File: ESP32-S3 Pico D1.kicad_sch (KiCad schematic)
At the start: 0 parts

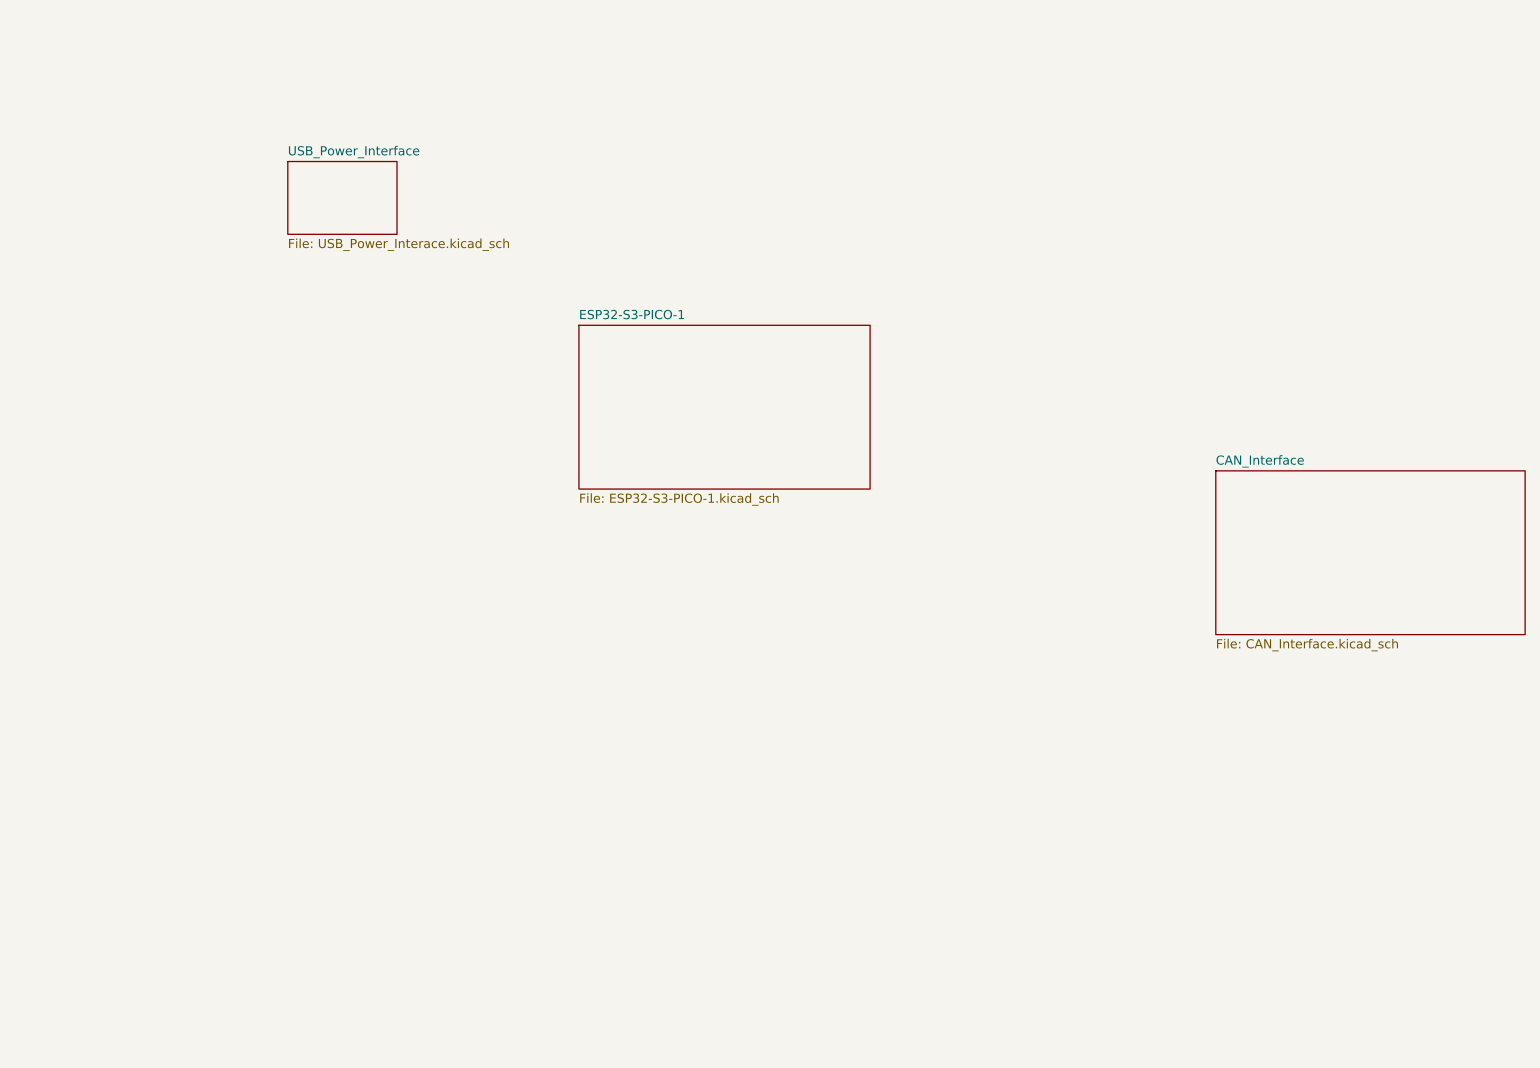
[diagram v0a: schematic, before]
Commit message: successful 1st pass, but I want to try some new bus'ing techniques to clean up the routing
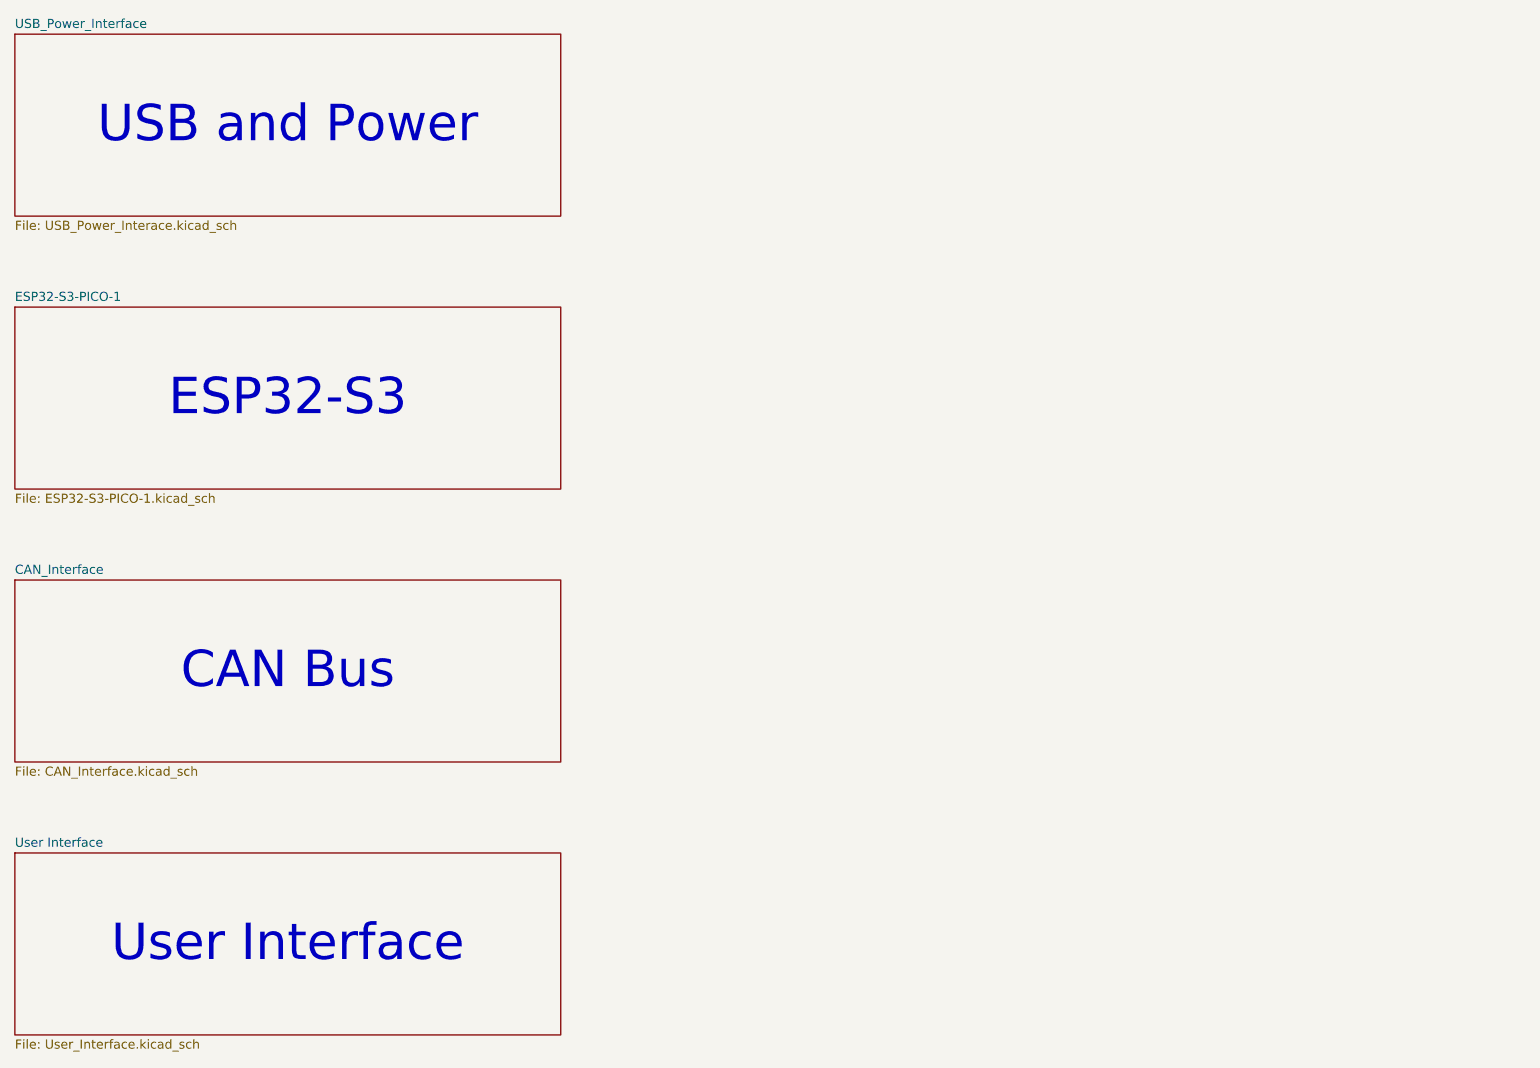
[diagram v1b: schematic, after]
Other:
- added sheet User Interface (User_Interface.kicad_sch)
- note added: "CAN Bus"
- note added: "ESP32-S3"
- note added: "USB and Power"
- note added: "User Interface"
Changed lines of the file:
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@@
 		(company "Rob Kean")
 	)
+	(text "ESP32-S3"
+		(exclude_from_sim no)
+		(at 88.9 88.9 0)
+		(effects
+			(font
+				(size 5.08 5.08)
+			)
+		)
+	)
+	(text "User Interface"
+		(exclude_from_sim no)
+		(at 88.9 165.1 0)
+		(effects
+			(font
+				(size 5.08 5.08)
+			)
+		)
+	)
+	(text "USB and Power"
+		(exclude_from_sim no)
+		(at 88.9 50.8 0)
+		(effects
+			(font
+				(size 5.08 5.08)
+			)
+		)
+	)
+	(text "CAN Bus"
+		(exclude_from_sim no)
+		(at 88.9 127 0)
+		(effects
+			(font
+				(size 5.08 5.08)
+			)
+		)
+	)
 	(sheet
-		(at 129.54 78.74)
-		(size 40.64 22.86)
+		(at 50.8 76.2)
+		(size 76.2 25.4)
 		(exclude_from_sim no)
 		(in_bom yes)
@@
 		)
 		(property "Sheetname" "ESP32-S3-PICO-1"
-			(at 129.54 78.0284 0)
+			(at 50.8 75.4884 0)
 			(effects
 				(font
@@
 		)
 		(property "Sheetfile" "ESP32-S3-PICO-1.kicad_sch"
-			(at 129.54 102.1846 0)
+			(at 50.8 102.1846 0)
 			(effects
 				(font
@@
 	)
 	(sheet
-		(at 218.44 99.06)
-		(size 43.18 22.86)
+		(at 50.8 114.3)
+		(size 76.2 25.4)
 		(exclude_from_sim no)
 		(in_bom yes)
@@
 		)
 		(property "Sheetname" "CAN_Interface"
-			(at 218.44 98.3484 0)
+			(at 50.8 113.5884 0)
 			(effects
 				(font
@@
 		)
 		(property "Sheetfile" "CAN_Interface.kicad_sch"
-			(at 218.44 122.5046 0)
+			(at 50.8 140.2846 0)
 			(effects
 				(font
@@
 	)
 	(sheet
-		(at 88.9 55.88)
-		(size 15.24 10.16)
+		(at 50.8 152.4)
+		(size 76.2 25.4)
+		(exclude_from_sim no)
+		(in_bom yes)
+		(on_board yes)
+		(dnp no)
+		(fields_autoplaced yes)
+		(stroke
+			(width 0.1524)
+			(type solid)
+		)
+		(fill
+			(color 0 0 0 0.0000)
+		)
+		(property "Sheetname" "User Interface"
+			(at 50.8 151.6884 0)
+			(effects
+				(font
+					(size 1.27 1.27)
+				)
+				(justify left bottom)
+			)
+		)
+		(property "Sheetfile" "User_Interface.kicad_sch"
+			(at 50.8 178.3846 0)
+			(effects
+				(font
+					(size 1.27 1.27)
+				)
+				(justify left top)
+			)
+		)
+		(instances
+			(project "ESP32-S3 Pico D1"
+				(path "/67f7b1e1-e87f-421a-8424-bb26889ab157"
+					(page "5")
+				)
+			)
+		)
+	)
+	(sheet
+		(at 50.8 38.1)
+		(size 76.2 25.4)
 		(exclude_from_sim no)
 		(in_bom yes)
@@
 		)
 		(property "Sheetname" "USB_Power_Interface"
-			(at 88.9 55.1684 0)
+			(at 50.8 37.3884 0)
 			(effects
 				(font
@@
 		)
 		(property "Sheetfile" "USB_Power_Interace.kicad_sch"
-			(at 88.9 66.6246 0)
+			(at 50.8 64.0846 0)
 			(effects
 				(font
